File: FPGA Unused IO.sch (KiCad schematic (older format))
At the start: 1 part, among them U1 xc7a50tftg256

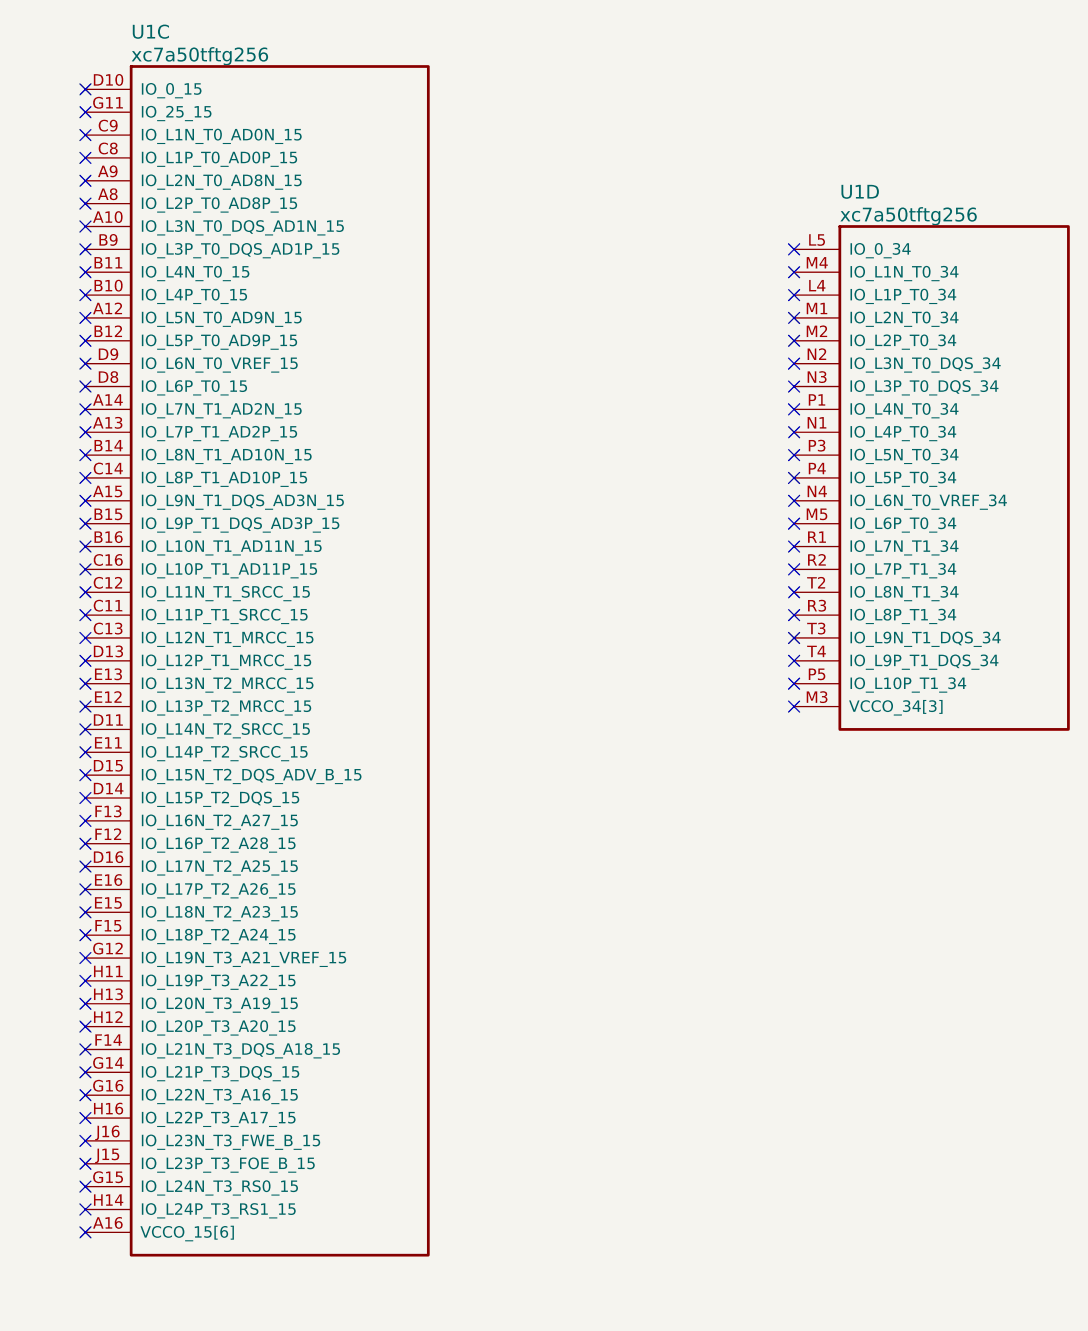
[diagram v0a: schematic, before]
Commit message: resolved ERC errors, and began assigning footprints
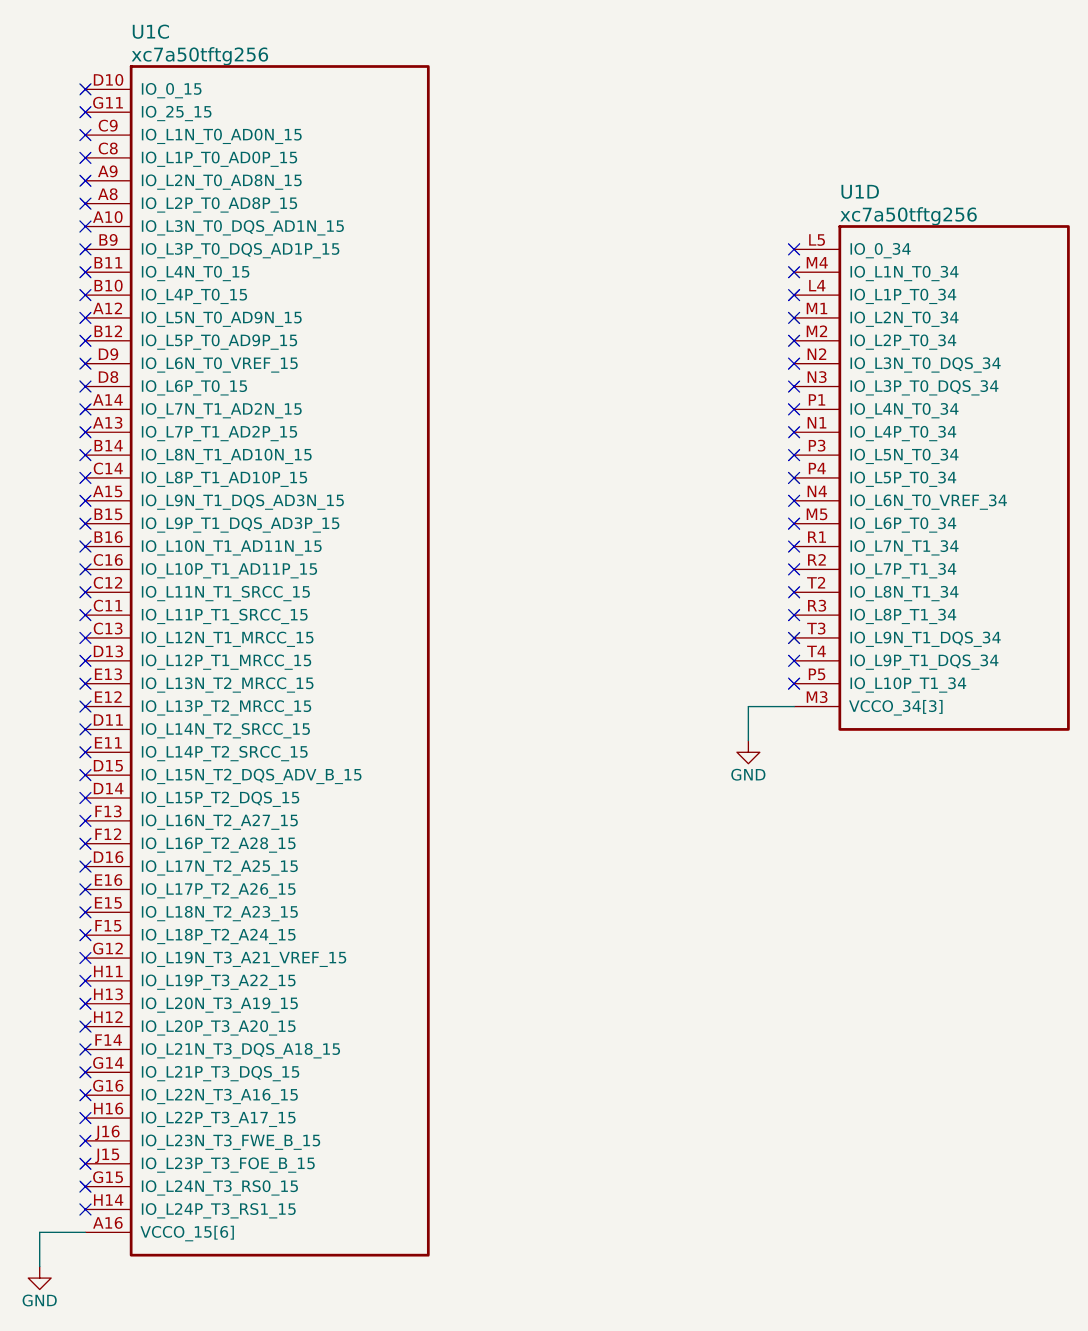
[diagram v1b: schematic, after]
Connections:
- net GND: now reaches U1.A16 (VCCO_15[6]), U1.B13 (VCCO_15[6]), U1.C10 (VCCO_15[6]), U1.E14 (VCCO_15[6]), U1.H15 (VCCO_15[6]), U1.J12 (VCCO_15[6])
- net GND: now also U1.M3 (VCCO_34[3]), U1.R4 (VCCO_34[3]), U1.T1 (VCCO_34[3])
- no-connect marks 72 -> 70
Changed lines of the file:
@@
 LIBS:N25Q128A
 LIBS:sparkfun
+LIBS:GSB3211311WEU
+LIBS:48258-0001
+LIBS:ArduinoSpecAn-cache
+LIBS:passiveelectret
+LIBS:passiveind
+LIBS:passiveinductor
+LIBS:fb_powerout
+LIBS:ferrite
+LIBS:df_device
 EELAYER 25 0
 EELAYER END
@@
 NoConn ~ 1850 6250
 NoConn ~ 1850 6350
-NoConn ~ 1850 6450
 $Comp
 L xc7a50tftg256 U1
@@
 	1    0    0    -1
 $EndComp
-NoConn ~ 4950 4150
+$Comp
+L GND #PWR018
+U 1 1 586E8826
+P 1650 6600
+F 0 "#PWR018" H 1650 6350 50  0001 C CNN
+F 1 "GND" H 1650 6450 50  0000 C CNN
+F 2 "" H 1650 6600 50  0000 C CNN
+F 3 "" H 1650 6600 50  0000 C CNN
+	1    1650 6600
+	1    0    0    -1
+$EndComp
+Wire Wire Line
+	1850 6450 1650 6450
+Wire Wire Line
+	1650 6450 1650 6600
+$Comp
+L GND #PWR019
+U 1 1 586E88A6
+P 4750 4300
+F 0 "#PWR019" H 4750 4050 50  0001 C CNN
+F 1 "GND" H 4750 4150 50  0000 C CNN
+F 2 "" H 4750 4300 50  0000 C CNN
+F 3 "" H 4750 4300 50  0000 C CNN
+	1    4750 4300
+	1    0    0    -1
+$EndComp
+Wire Wire Line
+	4950 4150 4750 4150
+Wire Wire Line
+	4750 4150 4750 4300
 $EndSCHEMATC

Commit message: A few more footprints
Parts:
- U1: footprint (none) -> SMD_Packages:BGA-256
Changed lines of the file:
@@
 F 0 "U1" H 2050 1700 60  0000 L CNN
 F 1 "xc7a50tftg256" H 2050 1600 60  0000 L CNN
-F 2 "" H 1850 1450 60  0001 C CNN
+F 2 "SMD_Packages:BGA-256" H 1850 1450 60  0001 C CNN
 F 3 "" H 1850 1450 60  0001 C CNN
 	3    1850 1450
@@
 F 0 "U1" H 5150 2400 60  0000 L CNN
 F 1 "xc7a50tftg256" H 5150 2300 60  0000 L CNN
-F 2 "" H 4950 2150 60  0001 C CNN
+F 2 "SMD_Packages:BGA-256" H 4950 2150 60  0001 C CNN
 F 3 "" H 4950 2150 60  0001 C CNN
 	4    4950 2150

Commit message: new annotation
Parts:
- U1: footprint SMD_Packages:BGA-256 -> (none)
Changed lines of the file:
@@
 F 0 "U1" H 2050 1700 60  0000 L CNN
 F 1 "xc7a50tftg256" H 2050 1600 60  0000 L CNN
-F 2 "SMD_Packages:BGA-256" H 1850 1450 60  0001 C CNN
+F 2 "" H 1850 1450 60  0001 C CNN
 F 3 "" H 1850 1450 60  0001 C CNN
 	3    1850 1450
@@
 F 0 "U1" H 5150 2400 60  0000 L CNN
 F 1 "xc7a50tftg256" H 5150 2300 60  0000 L CNN
-F 2 "SMD_Packages:BGA-256" H 4950 2150 60  0001 C CNN
+F 2 "" H 4950 2150 60  0001 C CNN
 F 3 "" H 4950 2150 60  0001 C CNN
 	4    4950 2150
@@
 $EndComp
 $Comp
-L GND #PWR018
+L GND #PWR18
 U 1 1 586E8826
 P 1650 6600
-F 0 "#PWR018" H 1650 6350 50  0001 C CNN
+F 0 "#PWR18" H 1650 6350 50  0001 C CNN
 F 1 "GND" H 1650 6450 50  0000 C CNN
 F 2 "" H 1650 6600 50  0000 C CNN
@@
 	1650 6450 1650 6600
 $Comp
-L GND #PWR019
+L GND #PWR19
 U 1 1 586E88A6
 P 4750 4300
-F 0 "#PWR019" H 4750 4050 50  0001 C CNN
+F 0 "#PWR19" H 4750 4050 50  0001 C CNN
 F 1 "GND" H 4750 4150 50  0000 C CNN
 F 2 "" H 4750 4300 50  0000 C CNN
